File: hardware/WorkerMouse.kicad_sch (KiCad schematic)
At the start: 13 parts, among them P1 USB_C_Plug_USB2.0, U1 ATtiny85-20P, Y1 16MHz

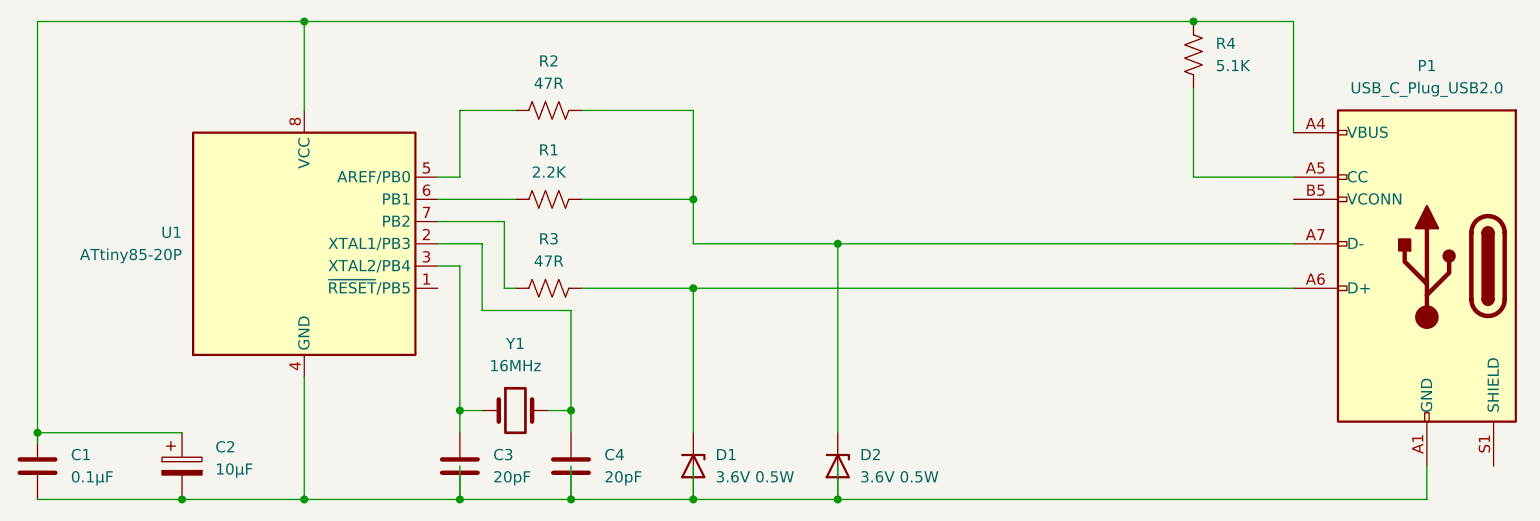
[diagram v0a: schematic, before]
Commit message: finish schema, add basic README
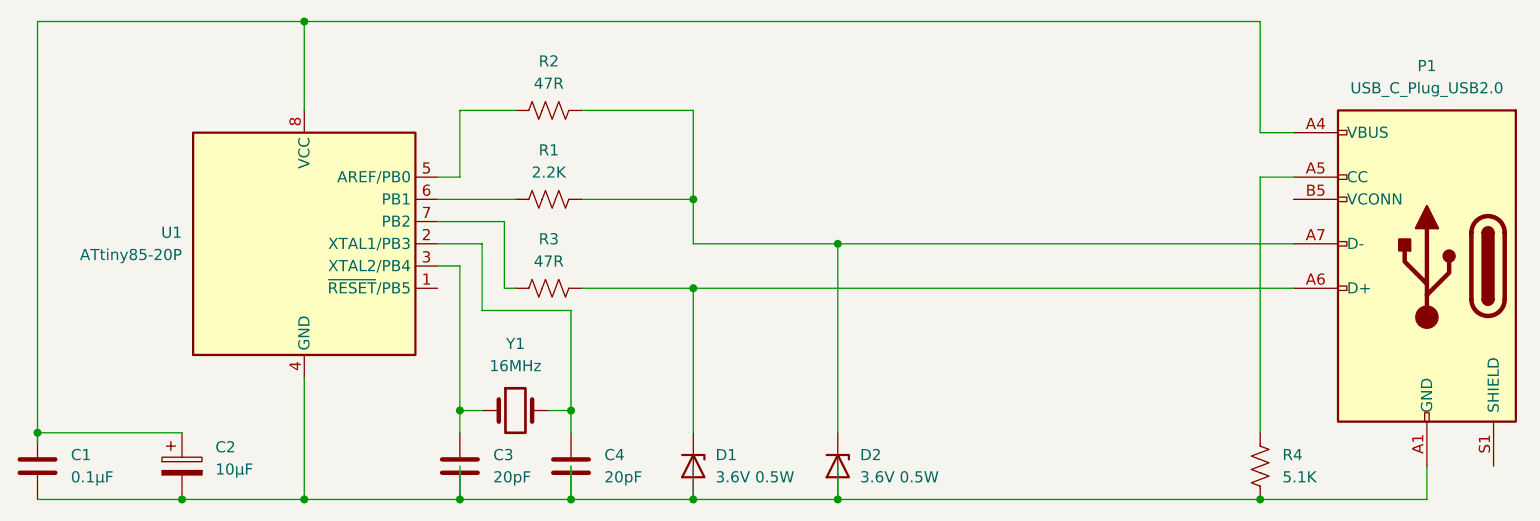
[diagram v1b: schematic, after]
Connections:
- net at C1.1, C2.1, P1.A4 (VBUS)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: no longer R4.1
- net at C1.2, C2.2, C3.2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: now also R4.2
- net at P1.A5 (CC): now also R4.1; no longer R4.2
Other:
- moved on the sheet: R4
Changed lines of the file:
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@@
   (junction (at 82.55 86.36) (diameter 0) (color 0 0 0 0)
   )
+  (junction (at 161.29 86.36) (diameter 0) (color 0 0 0 0)
+  )
   (junction (at 82.55 76.2) (diameter 0) (color 0 0 0 0)
   )
@@
   (junction (at 52.07 31.75) (diameter 0) (color 0 0 0 0)
   )
-  (junction (at 153.67 31.75) (diameter 0) (color 0 0 0 0)
-  )
   (junction (at 69.85 76.2) (diameter 0) (color 0 0 0 0)
   )
@@
     (stroke (width 0) (type default))
   )
-  (wire (pts (xy 52.07 31.75) (xy 153.67 31.75))
+  (wire (pts (xy 161.29 78.74) (xy 161.29 49.53))
+    (stroke (width 0) (type default))
+  )
+  (wire (pts (xy 52.07 31.75) (xy 161.29 31.75))
     (stroke (width 0) (type default))
   )
@@
     (stroke (width 0) (type default))
   )
-  (wire (pts (xy 153.67 31.75) (xy 165.1 31.75))
-    (stroke (width 0) (type default))
-  )
   (wire (pts (xy 96.52 62.23) (xy 165.1 62.23))
     (stroke (width 0) (type default))
@@
     (stroke (width 0) (type default))
   )
-  (wire (pts (xy 153.67 49.53) (xy 165.1 49.53))
+  (wire (pts (xy 161.29 44.45) (xy 165.1 44.45))
     (stroke (width 0) (type default))
   )
@@
     (stroke (width 0) (type default))
   )
-  (wire (pts (xy 153.67 39.37) (xy 153.67 49.53))
-    (stroke (width 0) (type default))
-  )
-  (wire (pts (xy 165.1 31.75) (xy 165.1 44.45))
+  (wire (pts (xy 161.29 31.75) (xy 161.29 44.45))
     (stroke (width 0) (type default))
   )
@@
     (stroke (width 0) (type default))
   )
+  (wire (pts (xy 161.29 49.53) (xy 165.1 49.53))
+    (stroke (width 0) (type default))
+  )
   (wire (pts (xy 76.2 41.91) (xy 69.85 41.91))
     (stroke (width 0) (type default))
@@
     (stroke (width 0) (type default))
   )
+  (wire (pts (xy 161.29 86.36) (xy 180.34 86.36))
+    (stroke (width 0) (type default))
+  )
+  (wire (pts (xy 113.03 86.36) (xy 161.29 86.36))
+    (stroke (width 0) (type default))
+  )
   (wire (pts (xy 96.52 86.36) (xy 96.52 82.55))
-    (stroke (width 0) (type default))
-  )
-  (wire (pts (xy 113.03 86.36) (xy 180.34 86.36))
     (stroke (width 0) (type default))
   )
@@
     )
   )
-  (symbol (lib_id "Device:R_US") (at 153.67 35.56 0) (unit 1)
+  (symbol (lib_id "Device:R_US") (at 161.29 82.55 0) (unit 1)
     (in_bom yes) (on_board yes) (dnp no) (fields_autoplaced)
-    (property "Reference" "R4" (at 156.21 34.29 0)
-      (effects (font (size 1.27 1.27)) (justify left))
-    )
-    (property "Value" "5.1K" (at 156.21 36.83 0)
-      (effects (font (size 1.27 1.27)) (justify left))
-    )
-    (property "Footprint" "" (at 154.686 35.814 90)
-      (effects (font (size 1.27 1.27)) hide)
-    )
-    (property "Datasheet" "~" (at 153.67 35.56 0)
-      (effects (font (size 1.27 1.27)) hide)
-    )
+    (property "Reference" "R4" (at 163.83 81.28 0)
+      (effects (font (size 1.27 1.27)) (justify left))
+    )
+    (property "Value" "5.1K" (at 163.83 83.82 0)
+      (effects (font (size 1.27 1.27)) (justify left))
+    )
+    (property "Footprint" "" (at 162.306 82.804 90)
+      (effects (font (size 1.27 1.27)) hide)
+    )
+    (property "Datasheet" "~" (at 161.29 82.55 0)
+      (effects (font (size 1.27 1.27)) hide)
+    )
